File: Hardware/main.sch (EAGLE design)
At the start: 40 parts, among them IC3 MEGA128-A, K1 DS2-L2-12V, T1 IRML5202, T2 IRML5202, T3 IRML5202, T4 IRML5202, U1 DS1307ZN+

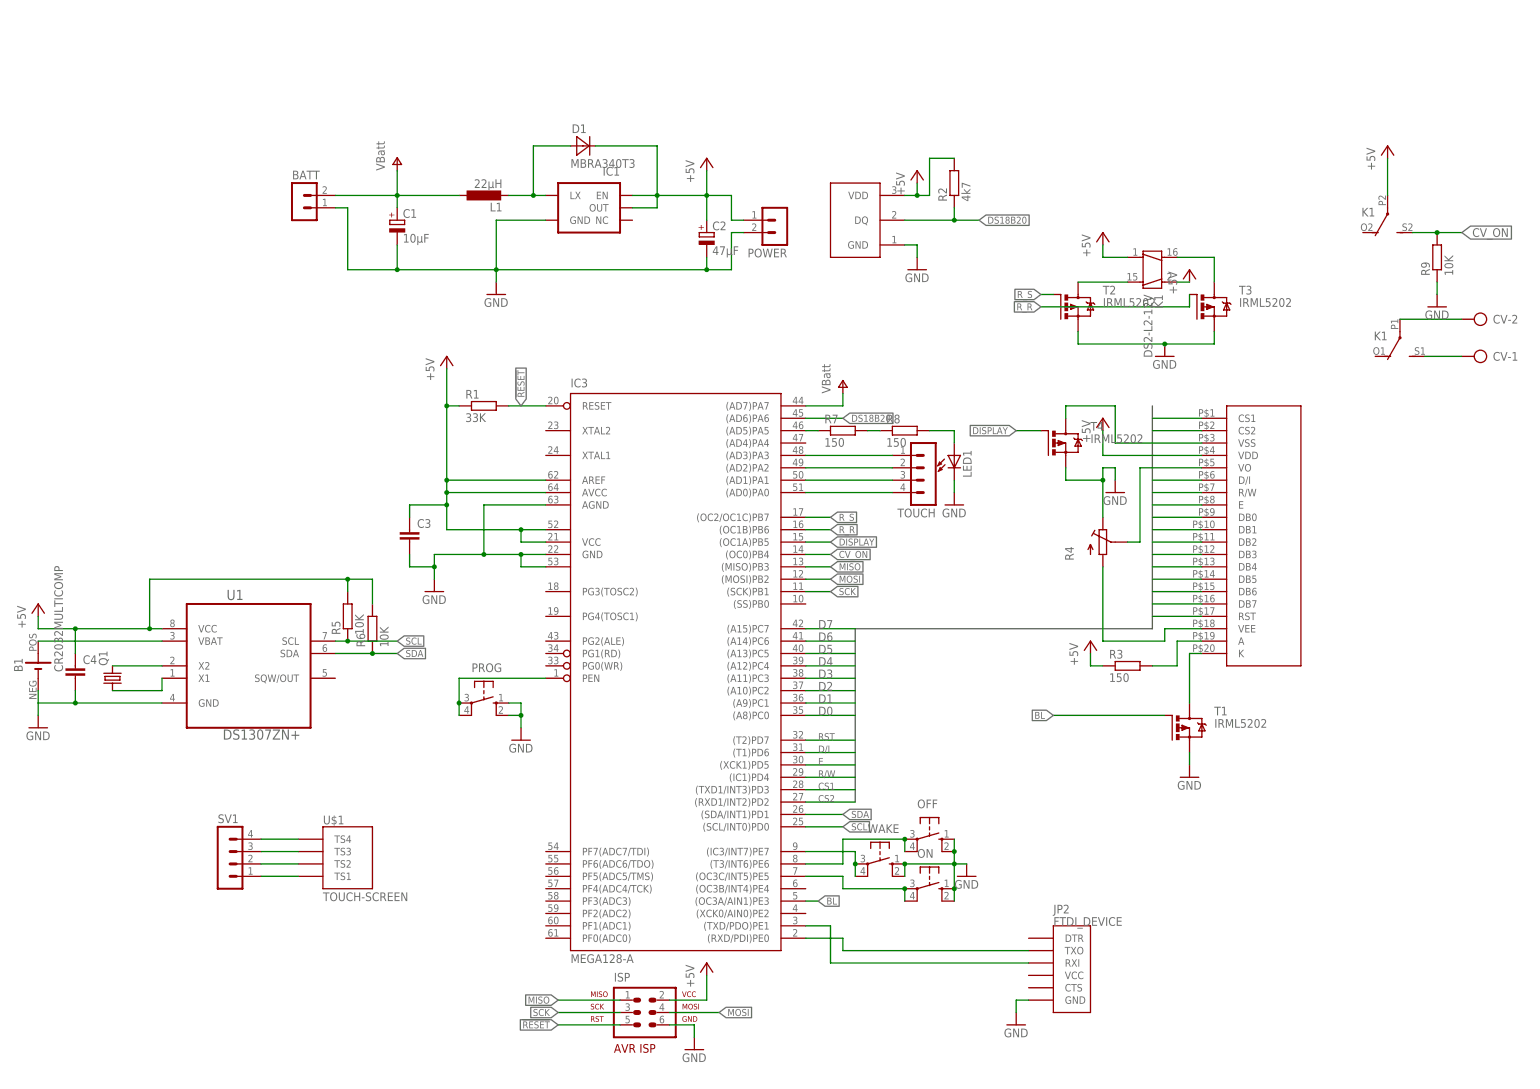
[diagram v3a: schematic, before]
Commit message: Added some extra components + bigger PCB
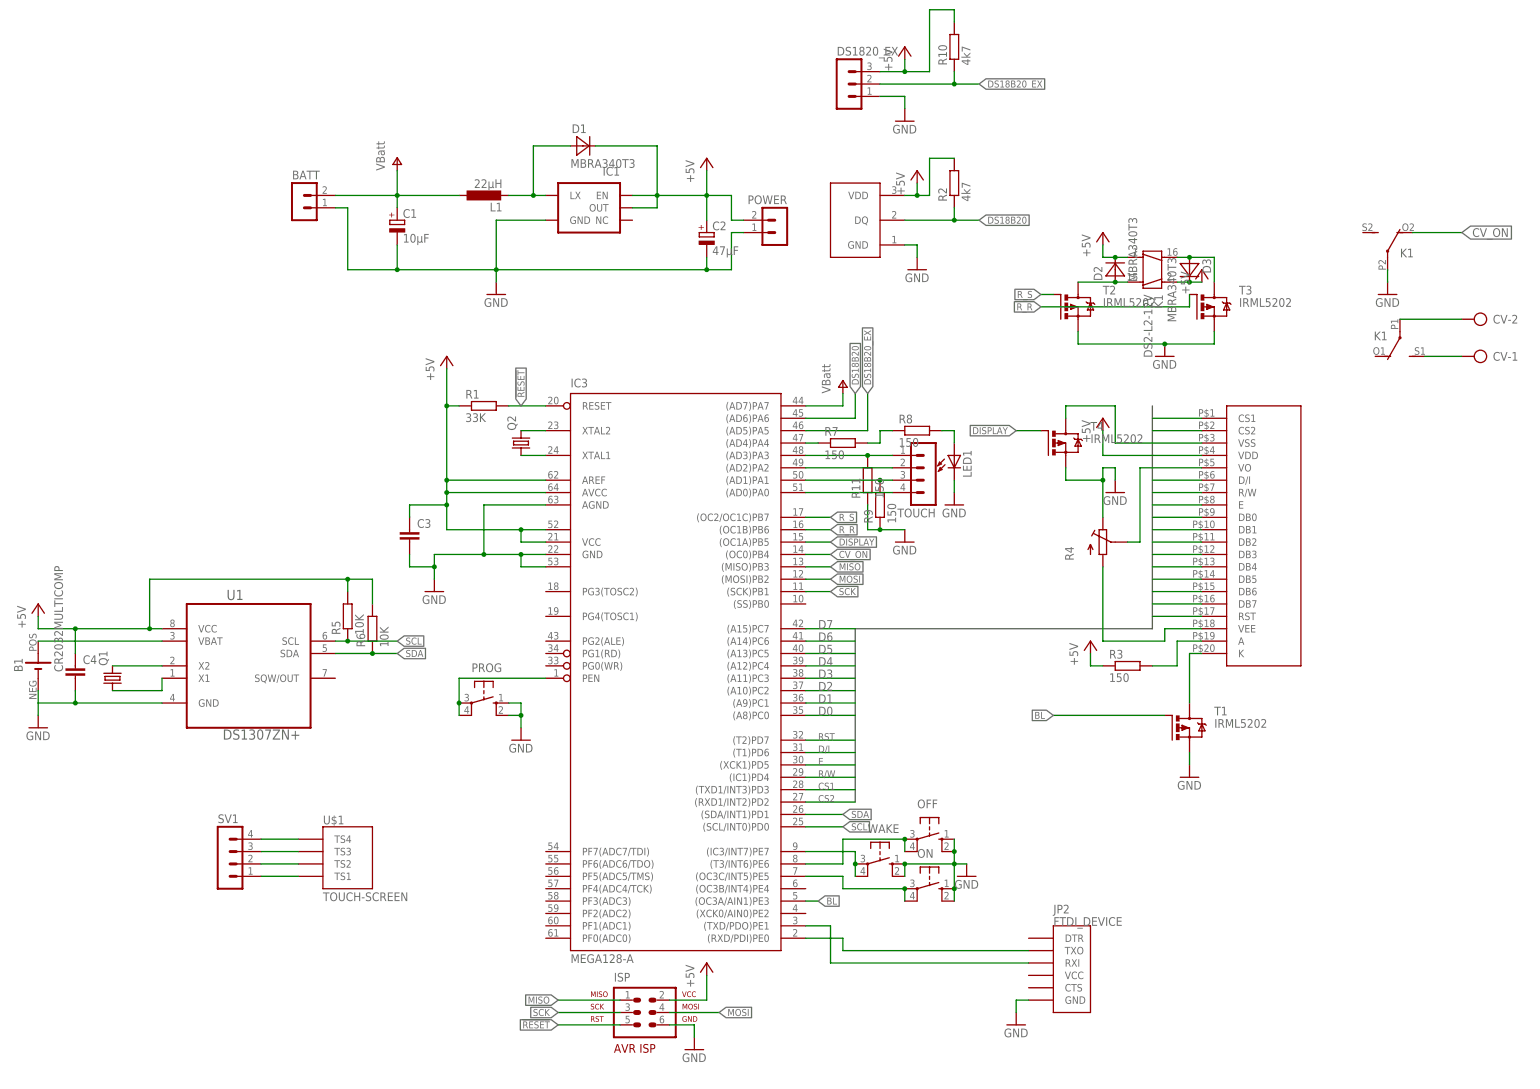
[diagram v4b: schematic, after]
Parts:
- added D2, D3: MBRA340T3, diode:MBRA340T3
- added DS1820_EX: (no value), con-lstb:MA03-1
- added Q2: (no value), crystal:CRYSTALSM49
- added R10: 4k7, rcl:R-EU_R0805
- added R11: 150, rcl:R-EU_R0805
- C2: device rcl:CPOL-EUF -> rcl:CPOL-EUD
- R9: value 10K -> 150
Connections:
- new net DS18B20_EX: DS1820_EX.2, IC3.(AD5)PA5, R10.1
- new net N$33: IC3.XTAL2, Q2.2
- new net N$34: IC3.XTAL1, Q2.1
- net +5V: now also D2.C, D3.C, DS1820_EX.3, POWER.4, R10.2; no longer K13.P, POWER.3
- net CV_ON: now also K13.O; no longer K13.S, R9.2
- net GND: now also DS1820_EX.1, K13.P, POWER.3, R11.1; no longer POWER.4
- net N$14: now also D2.A
- net N$15: now also D3.A
- net N$20: now also R9.2
- net N$22: now also R11.2
- net N$30: now also IC3.(AD4)PA4; no longer IC3.(AD5)PA5
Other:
- moved on the sheet: K1, POWER, R7, R8, R9

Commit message: This pcb version has been send to seeed.
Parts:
- added RESET: (no value), switch-omron:10-XX
- PROG: value (none) -> MA02-1; device switch-omron:10-XX -> con-lstb:MA02-1
- T1, T2, T3, T4: value IRML5202 -> IRLML2502PBF; device custom:IRML5202 -> custom:IRLML2502PBF
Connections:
- net !RESET: now also RESET.P, RESET.P1
- net GND: now also PROG.3, RESET.S, RESET.S1; no longer PROG.S, PROG.S1
- net N$8: now also PROG.4; no longer PROG.P, PROG.P1
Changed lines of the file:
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@@
 <part name="P+3" library="supply1" deviceset="+5V" device=""/>
 <part name="R1" library="rcl" deviceset="R-EU_" device="R0805" value="33K"/>
-<part name="PROG" library="switch-omron" deviceset="10-XX" device=""/>
+<part name="RESET" library="switch-omron" deviceset="10-XX" device=""/>
 <part name="R3" library="rcl" deviceset="R-EU_" device="R0805" value="150"/>
 <part name="P+4" library="supply1" deviceset="+5V" device=""/>
@@
 <part name="P+7" library="supply1" deviceset="+5V" device=""/>
 <part name="GND6" library="supply1" deviceset="GND" device=""/>
-<part name="T1" library="custom" deviceset="IRML5202" device=""/>
+<part name="T1" library="custom" deviceset="IRLML2502PBF" device=""/>
 <part name="GND7" library="supply1" deviceset="GND" device=""/>
 <part name="JP2" library="SparkFun-Connectors" deviceset="FTDI_DEVICE" device=""/>
@@
 <part name="GND9" library="supply1" deviceset="GND" device=""/>
 <part name="K1" library="relay" deviceset="DS2-L2-*" device="" technology="12V"/>
-<part name="T2" library="custom" deviceset="IRML5202" device=""/>
-<part name="T3" library="custom" deviceset="IRML5202" device=""/>
+<part name="T2" library="custom" deviceset="IRLML2502PBF" device=""/>
+<part name="T3" library="custom" deviceset="IRLML2502PBF" device=""/>
 <part name="P+9" library="supply1" deviceset="+5V" device=""/>
 <part name="P+10" library="supply1" deviceset="+5V" device=""/>
@@
 <part name="TOUCH" library="con-lstb" deviceset="MA04-1" device=""/>
 <part name="BATT" library="con-lstb" deviceset="MA02-1" device="" value=""/>
-<part name="T4" library="custom" deviceset="IRML5202" device=""/>
+<part name="T4" library="custom" deviceset="IRLML2502PBF" device=""/>
 <part name="U1" library="custom" deviceset="DS1307ZN+" device=""/>
 <part name="Q1" library="crystal" deviceset="CRYSTAL" device="TC26V"/>
@@
 <part name="R11" library="rcl" deviceset="R-EU_" device="R0805" value="150"/>
 <part name="GND15" library="supply1" deviceset="GND" device=""/>
+<part name="PROG" library="con-lstb" deviceset="MA02-1" device=""/>
+<part name="GND16" library="supply1" deviceset="GND" device=""/>
 </parts>
 <sheets>
@@
 <instance part="P+3" gate="1" x="5.08" y="132.08"/>
 <instance part="R1" gate="G$1" x="12.7" y="121.92"/>
-<instance part="PROG" gate="1" x="12.7" y="60.96" rot="R270"/>
+<instance part="RESET" gate="1" x="2.54" y="-5.08" rot="R270"/>
 <instance part="R3" gate="G$1" x="144.78" y="68.58"/>
 <instance part="P+4" gate="1" x="137.16" y="73.66"/>
 <instance part="IC3" gate="G$1" x="53.34" y="68.58"/>
-<instance part="GND3" gate="1" x="20.32" y="53.34"/>
+<instance part="GND3" gate="1" x="10.16" y="-12.7"/>
 <instance part="P+5" gate="1" x="86.36" y="127"/>
 <instance part="WAKE" gate="1" x="93.98" y="27.94" rot="R270"/>
@@
 <instance part="P+7" gate="1" x="101.6" y="170.18"/>
 <instance part="GND6" gate="1" x="101.6" y="149.86"/>
-<instance part="T1" gate="G$1" x="154.94" y="55.88"/>
+<instance part="T1" gate="G$1" x="154.94" y="55.88" rot="MR180"/>
 <instance part="GND7" gate="1" x="157.48" y="45.72"/>
 <instance part="JP2" gate="G$1" x="129.54" y="7.62"/>
@@
 <instance part="K1" gate="1" x="149.86" y="149.86" rot="R270"/>
 <instance part="K1" gate="2" x="200.66" y="137.16" rot="R180"/>
-<instance part="T2" gate="G$1" x="132.08" y="142.24"/>
-<instance part="T3" gate="G$1" x="160.02" y="142.24"/>
+<instance part="T2" gate="G$1" x="132.08" y="142.24" rot="MR180"/>
+<instance part="T3" gate="G$1" x="160.02" y="142.24" rot="MR180"/>
 <instance part="P+9" gate="1" x="139.7" y="157.48"/>
 <instance part="P+10" gate="1" x="160.02" y="149.86"/>
@@
 <instance part="TOUCH" gate="1" x="104.14" y="106.68" rot="R180"/>
 <instance part="BATT" gate="G$1" x="-25.4" y="165.1"/>
-<instance part="T4" gate="G$1" x="129.54" y="114.3"/>
+<instance part="T4" gate="G$1" x="129.54" y="114.3" rot="MR180"/>
 <instance part="U1" gate="A" x="-35.56" y="71.12"/>
 <instance part="Q1" gate="G$1" x="-63.5" y="66.04" rot="R90"/>
@@
 <instance part="R11" gate="G$1" x="91.44" y="106.68" rot="R90"/>
 <instance part="GND15" gate="1" x="99.06" y="93.98"/>
+<instance part="PROG" gate="G$1" x="2.54" y="66.04"/>
+<instance part="GND16" gate="1" x="12.7" y="58.42"/>
 </instances>
 <busses>
@@
 <segment>
 <pinref part="GND3" gate="1" pin="GND"/>
-<wire x1="20.32" y1="55.88" x2="20.32" y2="58.42" width="0.1524" layer="91"/>
-<pinref part="PROG" gate="1" pin="S1"/>
-<wire x1="20.32" y1="58.42" x2="20.32" y2="60.96" width="0.1524" layer="91"/>
-<wire x1="17.78" y1="58.42" x2="20.32" y2="58.42" width="0.1524" layer="91"/>
-<junction x="20.32" y="58.42"/>
-<pinref part="PROG" gate="1" pin="S"/>
-<wire x1="17.78" y1="60.96" x2="20.32" y2="60.96" width="0.1524" layer="91"/>
+<wire x1="10.16" y1="-10.16" x2="10.16" y2="-7.62" width="0.1524" layer="91"/>
+<pinref part="RESET" gate="1" pin="S1"/>
+<wire x1="10.16" y1="-7.62" x2="10.16" y2="-5.08" width="0.1524" layer="91"/>
+<wire x1="7.62" y1="-7.62" x2="10.16" y2="-7.62" width="0.1524" layer="91"/>
+<junction x="10.16" y="-7.62"/>
+<pinref part="RESET" gate="1" pin="S"/>
+<wire x1="7.62" y1="-5.08" x2="10.16" y2="-5.08" width="0.1524" layer="91"/>
 </segment>
 <segment>
@@
 <wire x1="93.98" y1="96.52" x2="99.06" y2="96.52" width="0.1524" layer="91"/>
 <junction x="93.98" y="96.52"/>
+</segment>
+<segment>
+<pinref part="PROG" gate="G$1" pin="3"/>
+<pinref part="GND16" gate="1" pin="GND"/>
+<wire x1="10.16" y1="63.5" x2="12.7" y2="63.5" width="0.1524" layer="91"/>
+<wire x1="12.7" y1="63.5" x2="12.7" y2="60.96" width="0.1524" layer="91"/>
 </segment>
 </net>
@@
 </segment>
 </net>
-<net name="N$8" class="0">
-<segment>
-<pinref part="IC3" gate="G$1" pin="PEN"/>
-<pinref part="PROG" gate="1" pin="P"/>
-<wire x1="25.4" y1="66.04" x2="7.62" y2="66.04" width="0.1524" layer="91"/>
-<wire x1="7.62" y1="66.04" x2="7.62" y2="60.96" width="0.1524" layer="91"/>
-<pinref part="PROG" gate="1" pin="P1"/>
-<wire x1="7.62" y1="60.96" x2="7.62" y2="58.42" width="0.1524" layer="91"/>
-<junction x="7.62" y="60.96"/>
-</segment>
-</net>
 <net name="N$10" class="0">
 <segment>
@@
 <label x="20.32" y="121.92" size="1.4224" layer="95" rot="R90" xref="yes"/>
 </segment>
+<segment>
+<pinref part="RESET" gate="1" pin="P"/>
+<wire x1="-2.54" y1="0" x2="-2.54" y2="-5.08" width="0.1524" layer="91"/>
+<pinref part="RESET" gate="1" pin="P1"/>
+<wire x1="-2.54" y1="-5.08" x2="-2.54" y2="-7.62" width="0.1524" layer="91"/>
+<junction x="-2.54" y="-5.08"/>
+<label x="-2.54" y="-5.08" size="1.4224" layer="95" rot="R90"/>
+</segment>
 </net>
 <net name="N$9" class="0">
@@
 <segment>
 <pinref part="T1" gate="G$1" pin="G"/>
-<wire x1="152.4" y1="58.42" x2="129.54" y2="58.42" width="0.1524" layer="91"/>
+<wire x1="149.86" y1="58.42" x2="129.54" y2="58.42" width="0.1524" layer="91"/>
 <label x="129.54" y="58.42" size="1.4224" layer="95" rot="R180" xref="yes"/>
 </segment>
@@
 <net name="R_S" class="0">
 <segment>
-<pinref part="T2" gate="G$1" pin="G"/>
-<wire x1="129.54" y1="144.78" x2="127" y2="144.78" width="0.1524" layer="91"/>
-<label x="127" y="144.78" size="1.4224" layer="95" rot="R180" xref="yes"/>
-</segment>
-<segment>
 <pinref part="IC3" gate="G$1" pin="(OC2/OC1C)PB7"/>
 <wire x1="78.74" y1="99.06" x2="83.82" y2="99.06" width="0.1524" layer="91"/>
 <label x="83.82" y="99.06" size="1.4224" layer="95" xref="yes"/>
 </segment>
+<segment>
+<pinref part="T2" gate="G$1" pin="G"/>
+<wire x1="127" y1="144.78" x2="124.46" y2="144.78" width="0.1524" layer="91"/>
+<label x="124.46" y="144.78" size="1.4224" layer="95" rot="R180" xref="yes"/>
+</segment>
 </net>
 <net name="R_R" class="0">
 <segment>
 <pinref part="T3" gate="G$1" pin="G"/>
-<wire x1="157.48" y1="144.78" x2="157.48" y2="142.24" width="0.1524" layer="91"/>
-<wire x1="157.48" y1="142.24" x2="127" y2="142.24" width="0.1524" layer="91"/>
-<label x="127" y="142.24" size="1.4224" layer="95" rot="R180" xref="yes"/>
+<wire x1="154.94" y1="144.78" x2="154.94" y2="142.24" width="0.1524" layer="91"/>
+<wire x1="154.94" y1="142.24" x2="124.46" y2="142.24" width="0.1524" layer="91"/>
+<label x="124.46" y="142.24" size="1.4224" layer="95" rot="R180" xref="yes"/>
 </segment>
 <segment>
@@
 <segment>
 <pinref part="T4" gate="G$1" pin="G"/>
-<wire x1="127" y1="116.84" x2="121.92" y2="116.84" width="0.1524" layer="91"/>
+<wire x1="124.46" y1="116.84" x2="121.92" y2="116.84" width="0.1524" layer="91"/>
 <label x="121.92" y="116.84" size="1.4224" layer="95" rot="R180" xref="yes"/>
 </segment>
@@
 </segment>
 </net>
+<net name="N$8" class="0">
+<segment>
+<pinref part="IC3" gate="G$1" pin="PEN"/>
+<wire x1="25.4" y1="66.04" x2="10.16" y2="66.04" width="0.1524" layer="91"/>
+<pinref part="PROG" gate="G$1" pin="4"/>
+</segment>
+</net>

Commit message: New programming header
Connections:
- removed net MISO: IC3.(MISO)PB3, ISP.1
- removed net MOSI: IC3.(MOSI)PB2, ISP.4
- removed net N$11: IC3.(RXD/PDI)PE0, JP2.TXO
- removed net N$2: IC3.(TXD/PDO)PE1, JP2.RXI
- new net PDI: IC3.(RXD/PDI)PE0, ISP.4, JP2.TXO
- new net PDO: IC3.(TXD/PDO)PE1, ISP.1, JP2.RXI
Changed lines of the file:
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@@
-</segment>
-</net>
-<net name="MOSI" class="0">
-<segment>
-<pinref part="ISP" gate="G$1" pin="4"/>
-<wire x1="50.8" y1="-2.54" x2="60.96" y2="-2.54" width="0.1524" layer="91"/>
-<label x="60.96" y="-2.54" size="1.4224" layer="95" xref="yes"/>
-</segment>
-<segment>
-<pinref part="IC3" gate="G$1" pin="(MOSI)PB2"/>
-<wire x1="78.74" y1="86.36" x2="83.82" y2="86.36" width="0.1524" layer="91"/>
-<label x="83.82" y="86.36" size="1.4224" layer="95" xref="yes"/>
-</segment>
-</net>
-<net name="MISO" class="0">
-<segment>
-<pinref part="ISP" gate="G$1" pin="1"/>
-<wire x1="40.64" y1="0" x2="27.94" y2="0" width="0.1524" layer="91"/>
-<label x="27.94" y="0" size="1.4224" layer="95" rot="R180" xref="yes"/>
-</segment>
-<segment>
-<pinref part="IC3" gate="G$1" pin="(MISO)PB3"/>
-<wire x1="78.74" y1="88.9" x2="83.82" y2="88.9" width="0.1524" layer="91"/>
-<label x="83.82" y="88.9" size="1.4224" layer="95" xref="yes"/>
 </segment>
 </net>
@@
 </segment>
 </net>
-<net name="N$2" class="0">
+<net name="PDO" class="0">
 <segment>
 <pinref part="JP2" gate="G$1" pin="RXI"/>
-<wire x1="124.46" y1="7.62" x2="83.82" y2="7.62" width="0.1524" layer="91"/>
+<wire x1="124.46" y1="7.62" x2="96.52" y2="7.62" width="0.1524" layer="91"/>
+<wire x1="96.52" y1="7.62" x2="83.82" y2="7.62" width="0.1524" layer="91"/>
 <wire x1="83.82" y1="7.62" x2="83.82" y2="15.24" width="0.1524" layer="91"/>
 <pinref part="IC3" gate="G$1" pin="(TXD/PDO)PE1"/>
 <wire x1="83.82" y1="15.24" x2="78.74" y2="15.24" width="0.1524" layer="91"/>
+<wire x1="96.52" y1="7.62" x2="96.52" y2="2.54" width="0.1524" layer="91"/>
+<junction x="96.52" y="7.62"/>
+<label x="96.52" y="2.54" size="1.4224" layer="95" rot="R270" xref="yes"/>
+</segment>
+<segment>
+<pinref part="ISP" gate="G$1" pin="1"/>
+<wire x1="40.64" y1="0" x2="27.94" y2="0" width="0.1524" layer="91"/>
+<label x="27.94" y="0" size="1.4224" layer="95" rot="R180" xref="yes"/>
 </segment>
 </net>
-<net name="N$11" class="0">
+<net name="PDI" class="0">
 <segment>
 <pinref part="IC3" gate="G$1" pin="(RXD/PDI)PE0"/>
@@
 <wire x1="86.36" y1="12.7" x2="86.36" y2="10.16" width="0.1524" layer="91"/>
 <pinref part="JP2" gate="G$1" pin="TXO"/>
-<wire x1="86.36" y1="10.16" x2="124.46" y2="10.16" width="0.1524" layer="91"/>
+<wire x1="86.36" y1="10.16" x2="93.98" y2="10.16" width="0.1524" layer="91"/>
+<wire x1="93.98" y1="10.16" x2="124.46" y2="10.16" width="0.1524" layer="91"/>
+<wire x1="93.98" y1="10.16" x2="93.98" y2="2.54" width="0.1524" layer="91"/>
+<junction x="93.98" y="10.16"/>
+<label x="93.98" y="2.54" size="1.4224" layer="95" rot="R270" xref="yes"/>
+</segment>
+<segment>
+<pinref part="ISP" gate="G$1" pin="4"/>
+<wire x1="50.8" y1="-2.54" x2="60.96" y2="-2.54" width="0.1524" layer="91"/>
+<label x="60.96" y="-2.54" size="1.4224" layer="95" xref="yes"/>
 </segment>
 </net>
